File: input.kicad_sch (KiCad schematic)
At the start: 5 parts, among them J5 AudioJack2_SwitchT, J6 Conn_02x04_Odd_Even

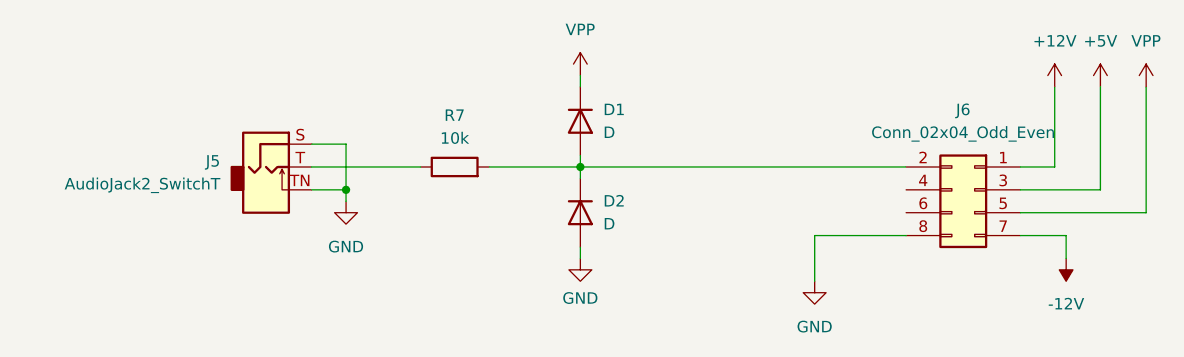
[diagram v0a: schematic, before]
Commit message: Switched to two layers
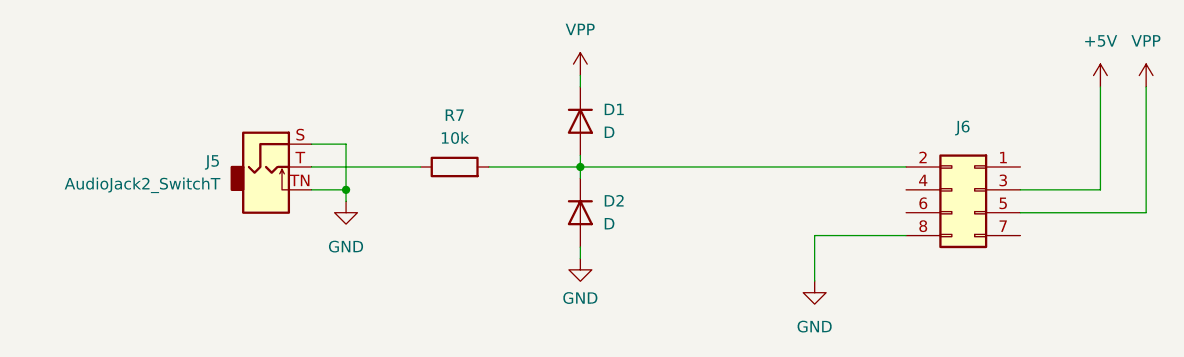
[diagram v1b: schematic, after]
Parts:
- J6: value Conn_02x04_Odd_Even -> (none)
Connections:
- net +12V: no longer names the net of J6.1 (Pin_1)
- net -12V: no longer names the net of J6.7 (Pin_7)
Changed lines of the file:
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@@
-    (stroke (width 0) (type default) (color 0 0 0 0))
-  )
-  (wire (pts (xy 200.66 89.535) (xy 205.74 89.535))
     (stroke (width 0) (type default) (color 0 0 0 0))
   )
   (wire (pts (xy 151.765 92.075) (xy 151.765 90.805))
-    (stroke (width 0) (type default) (color 0 0 0 0))
-  )
-  (wire (pts (xy 204.47 73.025) (xy 204.47 81.915))
     (stroke (width 0) (type default) (color 0 0 0 0))
   )
@@
   )
   (wire (pts (xy 121.92 79.375) (xy 125.73 79.375))
-    (stroke (width 0) (type default) (color 0 0 0 0))
-  )
-  (wire (pts (xy 205.74 89.535) (xy 205.74 92.075))
     (stroke (width 0) (type default) (color 0 0 0 0))
   )
@@
     (stroke (width 0) (type default) (color 0 0 0 0))
   )
-  (wire (pts (xy 200.66 81.915) (xy 204.47 81.915))
-    (stroke (width 0) (type default) (color 0 0 0 0))
-  )
   (wire (pts (xy 187.96 81.915) (xy 151.765 81.915))
     (stroke (width 0) (type default) (color 0 0 0 0))
@@
   (wire (pts (xy 151.765 81.915) (xy 151.765 83.185))
     (stroke (width 0) (type default) (color 0 0 0 0))
-  )
-  (symbol (lib_id "power:+12V") (at 204.47 73.025 0) (unit 1)
-    (in_bom yes) (on_board yes) (fields_autoplaced)
-    (property "Reference" "#PWR0103" (id 0) (at 204.47 76.835 0)
-      (effects (font (size 1.27 1.27)) hide)
-    )
-    (property "Value" "+12V" (id 1) (at 204.47 67.945 0))
-    (property "Footprint" "" (id 2) (at 204.47 73.025 0)
-      (effects (font (size 1.27 1.27)) hide)
-    )
-    (property "Datasheet" "" (id 3) (at 204.47 73.025 0)
-      (effects (font (size 1.27 1.27)) hide)
-    )
-    (pin "1")
   )
   (symbol (lib_id "power:GND") (at 177.8 94.615 0) (unit 1)
@@
     (pin "1")
     (pin "2")
-  )
-  (symbol (lib_id "power:-12V") (at 205.74 92.075 180) (unit 1)
-    (in_bom yes) (on_board yes) (fields_autoplaced)
-    (property "Reference" "#PWR0102" (id 0) (at 205.74 94.615 0)
-      (effects (font (size 1.27 1.27)) hide)
-    )
-    (property "Value" "-12V" (id 1) (at 205.74 97.155 0))
-    (property "Footprint" "" (id 2) (at 205.74 92.075 0)
-      (effects (font (size 1.27 1.27)) hide)
-    )
-    (property "Datasheet" "" (id 3) (at 205.74 92.075 0)
-      (effects (font (size 1.27 1.27)) hide)
-    )
-    (pin "1")
   )
   (symbol (lib_id "Device:D") (at 151.765 86.995 270) (unit 1)
@@
   (symbol (lib_id "Connector_Generic:Conn_02x04_Odd_Even") (at 195.58 84.455 0) (mirror y) (unit 1)
     (in_bom yes) (on_board yes) (fields_autoplaced)
-    (property "Reference" "J6" (id 0) (at 194.31 75.565 0))
-    (property "Value" "Conn_02x04_Odd_Even" (id 1) (at 194.31 78.105 0))
+    (property "Reference" "J6" (id 0) (at 194.31 77.47 0))
+    (property "Value" "" (id 1) (at 194.31 78.105 0)
+      (effects (font (size 1.27 1.27)) hide)
+    )
     (property "Footprint" "Connector_PinHeader_2.54mm:PinHeader_2x04_P2.54mm_Vertical" (id 2) (at 195.58 84.455 0)
       (effects (font (size 1.27 1.27)) hide)
